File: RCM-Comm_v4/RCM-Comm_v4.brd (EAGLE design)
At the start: 50.8 x 66 mm, 30 parts, among them J1 BLACKFIN_HEADER, J2 2199230-4

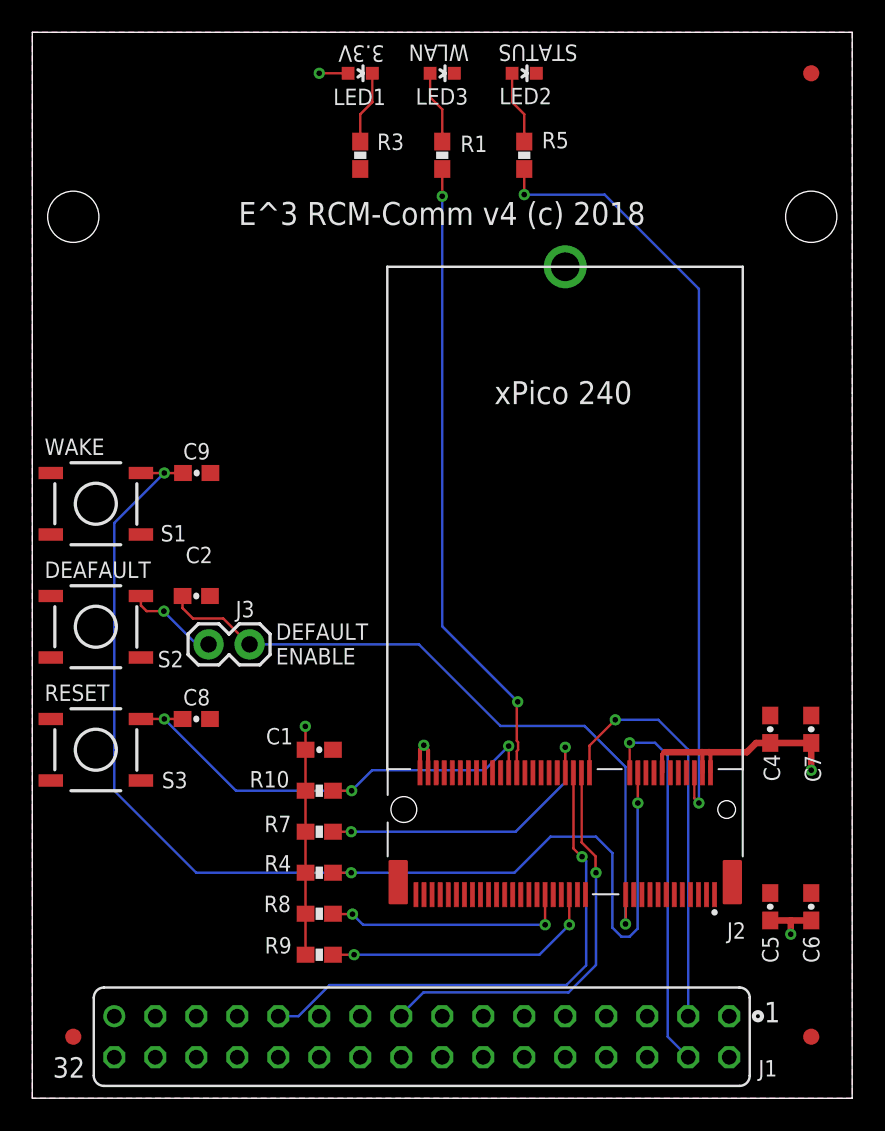
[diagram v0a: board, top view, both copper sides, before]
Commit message: Updated final BOM. Final 'd' version of gerbers, which got sent to JLCPCB.
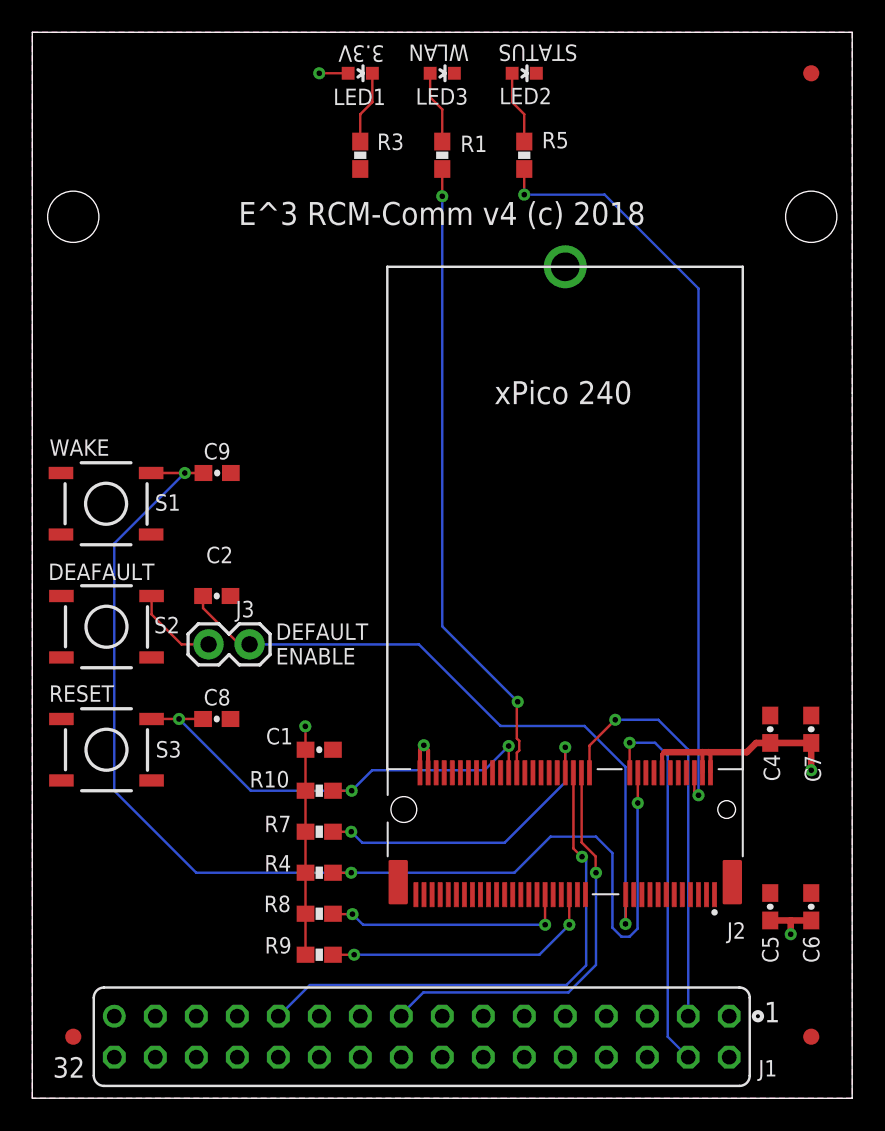
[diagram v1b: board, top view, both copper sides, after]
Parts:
- moved C2 1.27 mm to (14.0, 31.1)
- moved C8 1.27 mm to (14.0, 23.5)
- moved C9 1.27 mm to (14.0, 38.7)
- moved S2 0.66 mm to (7.14, 29.2)
- moved S3 0.66 mm to (7.14, 21.6)
- moved S1 0.63 mm to (7.11, 36.8)
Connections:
- removed net N$24: J1.6
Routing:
- net !DEFAULT!: track 43.9 -> 42.6 mm
- net WKUP: track 75.3 -> 76.5 mm
- net STATUS_LED: track 48.7 -> 47.7 mm
- net NTRST: track 19.4 -> 20.0 mm
- net N$1: track 5.79 -> 5.44 mm, vias 1 -> 0
